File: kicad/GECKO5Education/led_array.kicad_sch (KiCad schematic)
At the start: 181 parts, among them Q1 BC807, U4 74HC154BQ,118, U6 LFE5U-85F-6BG381x

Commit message: Final version
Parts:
- renumbered C15 to C22, D2 to D10, D2 to D100, D2 to D101, D2 to D102, D2 to D103, D2 to D104, D2 to D105, D2 to D106, D2 to D107, D2 to D108, D2 to D109, D2 to D11, D2 to D110, D2 to D111, D2 to D112, D2 to D113, D2 to D114, D2 to D115, D2 to D116, D2 to D117, D2 to D118, D2 to D119, D2 to D12, D2 to D120, D2 to D121, D2 to D13, D2 to D14, D2 to D15, D2 to D16, D2 to D17, D2 to D18, D2 to D19, D2 to D20, D2 to D21, D2 to D22, D2 to D23, D2 to D24, D2 to D25, D2 to D26, D2 to D27, D2 to D28, D2 to D29, D2 to D3, D2 to D30, D2 to D31, D2 to D32, D2 to D33, D2 to D34, D2 to D35, D2 to D36, D2 to D37, D2 to D38, D2 to D39, D2 to D4, D2 to D40, D2 to D41, D2 to D42, D2 to D43, D2 to D44, D2 to D45, D2 to D46, D2 to D47, D2 to D48, D2 to D49, D2 to D5, D2 to D50, D2 to D51, D2 to D52, D2 to D53, D2 to D54, D2 to D55, D2 to D56, D2 to D57, D2 to D58, D2 to D59, D2 to D6, D2 to D60, D2 to D61, D2 to D62, D2 to D63, D2 to D64, D2 to D65, D2 to D66, D2 to D67, D2 to D68, D2 to D69, D2 to D7, D2 to D70, D2 to D71, D2 to D72, D2 to D73, D2 to D74, D2 to D75, D2 to D76, D2 to D77, D2 to D78, D2 to D79, D2 to D8, D2 to D80, D2 to D81, D2 to D82, D2 to D83, D2 to D84, D2 to D85, D2 to D86, D2 to D87, D2 to D88, D2 to D89, D2 to D9, D2 to D90, D2 to D91, D2 to D92, D2 to D93, D2 to D94, D2 to D95, D2 to D96, D2 to D97, D2 to D98, D2 to D99, Q1 to Q10, Q1 to Q11, Q1 to Q12, Q1 to Q13, Q1 to Q14, Q1 to Q15, Q1 to Q16, Q1 to Q17, Q1 to Q6, Q1 to Q7, Q1 to Q8, Q1 to Q9, R1 to R48, R1 to R49, R1 to R50, R1 to R51, R1 to R52, R1 to R53, R1 to R54, R1 to R55, R1 to R56, R1 to R57, R1 to R58, R1 to R59, R1 to R60, R1 to R61, R1 to R62, R1 to R63, R1 to R64, R1 to R65, R1 to R66, R1 to R67, R1 to R68, R1 to R69, R1 to R70, R1 to R71, R1 to R72, R1 to R73, R1 to R74, R1 to R75, R1 to R76, R1 to R77, R1 to R78, R1 to R79, R1 to R80, R1 to R81, R1 to R82, R1 to R83, R1 to R84, R1 to R85, R1 to R86, R1 to R87, R1 to R88, R1 to R89, R1 to R90, R1 to R91, R1 to R92, R1 to R93, U4 to U5

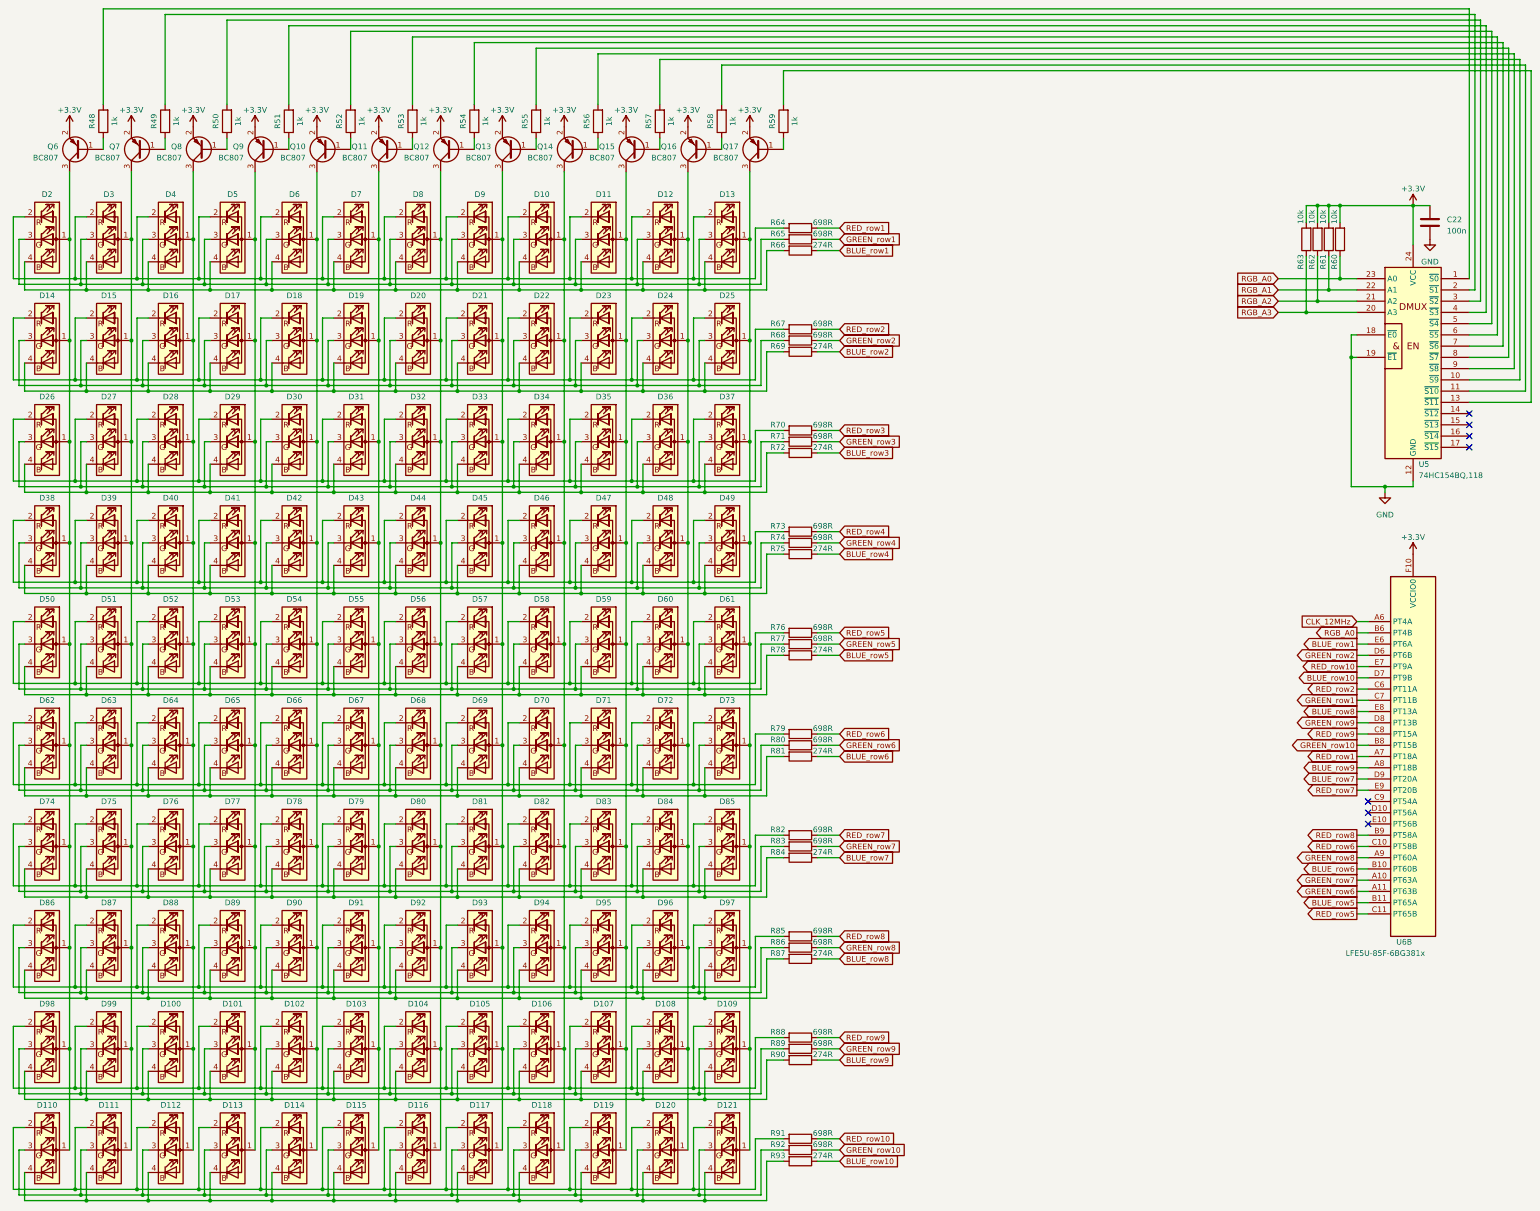
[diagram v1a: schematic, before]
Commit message: Switched to less expensive RGB-Leds
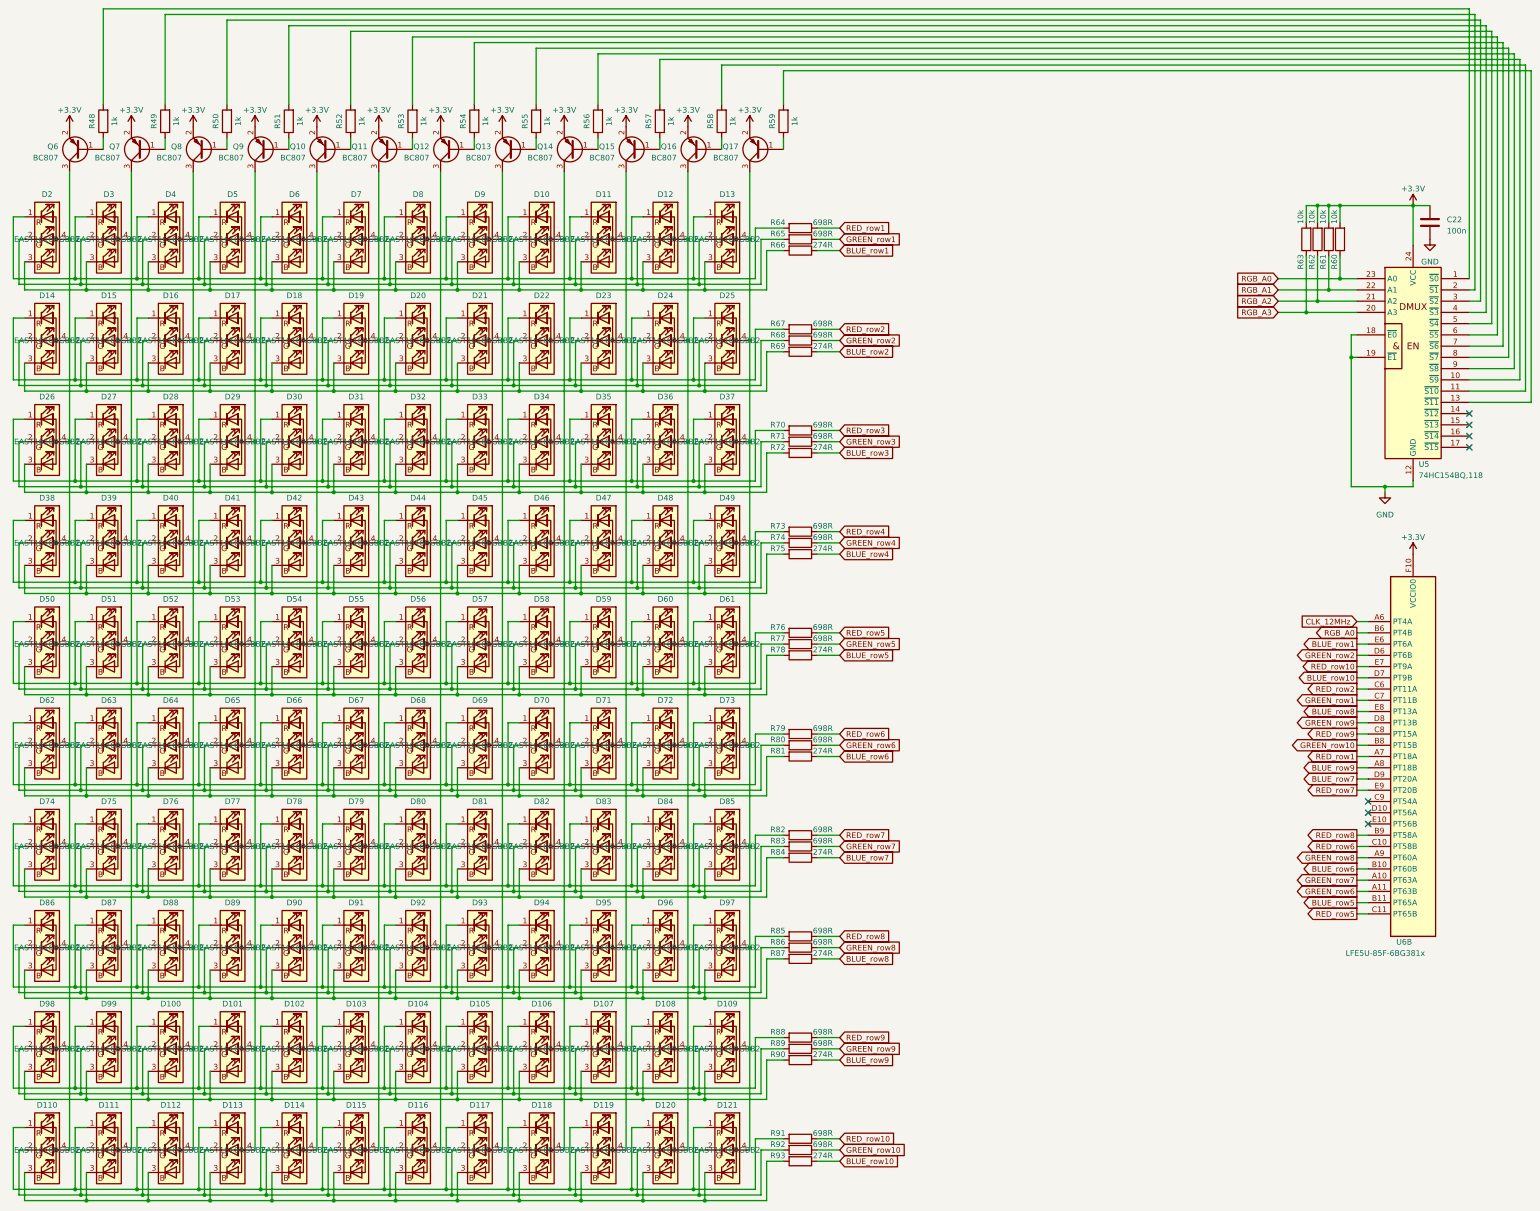
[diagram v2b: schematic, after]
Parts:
- D10, D100, D101, D102, D103, D104, D105, D106, D107, D108, D109, D11, D110, D111, D112, D113, D114, D115, D116, D117, D118, D119, D12, D120, D121, D13, D14, D15, D16, D17, D18, D19, D2, D20, D21, D22, D23, D24, D25, D26, D27, D28, D29, D3, D30, D31, D32, D33, D34, D35, D36, D37, D38, D39, D4, D40, D41, D42, D43, D44, D45, D46, D47, D48, D49, D5, D50, D51, D52, D53, D54, D55, D56, D57, D58, D59, D6, D60, D61, D62, D63, D64, D65, D66, D67, D68, D69, D7, D70, D71, D72, D73, D74, D75, D76, D77, D78, D79, D8, D80, D81, D82, D83, D84, D85, D86, D87, D88, D89, D9, D90, D91, D92, D93, D94, D95, D96, D97, D98, D99: value XZCMEDGCBD110W -> EAST1616RGBB2; footprint gecko4education:RGB_LED -> gecko4education:EAST1616RGBB2_EVE; symbol Device:LED_ARGB -> gecko5education:EAST1616RGBB2
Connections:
- net at D74.2, D75.2, D76.2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: now also R83.2; no longer R82.2
- net at D74.3, D75.3, D76.3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: now also R84.2; no longer R83.2
- net at D14.2, D15.2, D16.2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: now also R68.2; no longer R67.2
- net at D14.3, D15.3, D16.3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: now also R69.2; no longer R68.2
- net at D86.3, D87.3, D88.3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: now also R87.2; no longer R86.2
- net at D62.2, D63.2, D64.2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: now also R80.2; no longer R79.2
- net at D62.3, D63.3, D64.3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: now also R81.2; no longer R80.2
- net at D26.2, D27.2, D28.2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: now also R71.2; no longer R70.2
- net at D10.2, D11.2, D12.2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: now also R65.2; no longer R64.2
- net at D10.3, D11.3, D12.3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: now also R66.2; no longer R65.2
- net at D50.3, D51.3, D52.3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: now also R78.2; no longer R77.2
- net at D38.2, D39.2, D40.2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: now also R74.2; no longer R73.2
- net at D38.3, D39.3, D40.3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: now also R75.2; no longer R74.2
- net at D26.3, D27.3, D28.3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: now also R72.2; no longer R71.2
- net at D100.2, D101.2, D102.2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: now also R89.2; no longer R88.2
- net at D100.3, D101.3, D102.3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: now also R90.2; no longer R89.2
- net at D110.2, D111.2, D112.2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: now also R92.2; no longer R91.2
- net at D110.3, D111.3, D112.3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: now also R93.2; no longer R92.2
- net at D50.2, D51.2, D52.2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: now also R77.2; no longer R76.2
- net at D86.2, D87.2, D88.2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: now also R86.2; no longer R85.2
- new net: D74.1, D75.1, D76.1, D77.1, D78.1, D79.1, D80.1, D81.1, D82.1, D83.1, D84.1, D85.1, R82.2
- new net: D107.4, D11.4, D119.4, D23.4, D35.4, D47.4, D59.4, D71.4, D83.4, D95.4, Q15.3 (C)
- new net: D14.1, D15.1, D16.1, D17.1, D18.1, D19.1, D20.1, D21.1, D22.1, D23.1, D24.1, D25.1, R67.2
- new net: D108.4, D12.4, D120.4, D24.4, D36.4, D48.4, D60.4, D72.4, D84.4, D96.4, Q16.3 (C)
- new net: D62.1, D63.1, D64.1, D65.1, D66.1, D67.1, D68.1, D69.1, D70.1, D71.1, D72.1, D73.1, R79.2
- new net: D100.4, D112.4, D16.4, D28.4, D4.4, D40.4, D52.4, D64.4, D76.4, D88.4, Q8.3 (C)
- new net: D26.1, D27.1, D28.1, D29.1, D30.1, D31.1, D32.1, D33.1, D34.1, D35.1, D36.1, D37.1, R70.2
- new net: D10.1, D11.1, D12.1, D13.1, D2.1, D3.1, D4.1, D5.1, D6.1, D7.1, D8.1, D9.1, R64.2
- new net: D102.4, D114.4, D18.4, D30.4, D42.4, D54.4, D6.4, D66.4, D78.4, D90.4, Q10.3 (C)
- new net: D38.1, D39.1, D40.1, D41.1, D42.1, D43.1, D44.1, D45.1, D46.1, D47.1, D48.1, D49.1, R73.2
- new net: D110.4, D14.4, D2.4, D26.4, D38.4, D50.4, D62.4, D74.4, D86.4, D98.4, Q6.3 (C)
- new net: D104.4, D116.4, D20.4, D32.4, D44.4, D56.4, D68.4, D8.4, D80.4, D92.4, Q12.3 (C)
- new net: D103.4, D115.4, D19.4, D31.4, D43.4, D55.4, D67.4, D7.4, D79.4, D91.4, Q11.3 (C)
- new net: D105.4, D117.4, D21.4, D33.4, D45.4, D57.4, D69.4, D81.4, D9.4, D93.4, Q13.3 (C)
- new net: D101.4, D113.4, D17.4, D29.4, D41.4, D5.4, D53.4, D65.4, D77.4, D89.4, Q9.3 (C)
- new net: D100.1, D101.1, D102.1, D103.1, D104.1, D105.1, D106.1, D107.1, D108.1, D109.1, D98.1, D99.1, R88.2
- new net: D10.4, D106.4, D118.4, D22.4, D34.4, D46.4, D58.4, D70.4, D82.4, D94.4, Q14.3 (C)
- new net: D110.1, D111.1, D112.1, D113.1, D114.1, D115.1, D116.1, D117.1, D118.1, D119.1, D120.1, D121.1, R91.2
- new net: D50.1, D51.1, D52.1, D53.1, D54.1, D55.1, D56.1, D57.1, D58.1, D59.1, D60.1, D61.1, R76.2
- new net: D109.4, D121.4, D13.4, D25.4, D37.4, D49.4, D61.4, D73.4, D85.4, D97.4, Q17.3 (C)
- new net: D111.4, D15.4, D27.4, D3.4, D39.4, D51.4, D63.4, D75.4, D87.4, D99.4, Q7.3 (C)
- new net: D86.1, D87.1, D88.1, D89.1, D90.1, D91.1, D92.1, D93.1, D94.1, D95.1, D96.1, D97.1, R85.2
